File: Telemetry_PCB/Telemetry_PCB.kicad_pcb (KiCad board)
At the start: 2 copper layers, 27.9 x 18.5 mm, 7 parts, among them J1 Raspberry Pi Zero W, J2 Voltage Sensor, J3 Current Sensor, J4 ADC, J5 GPS

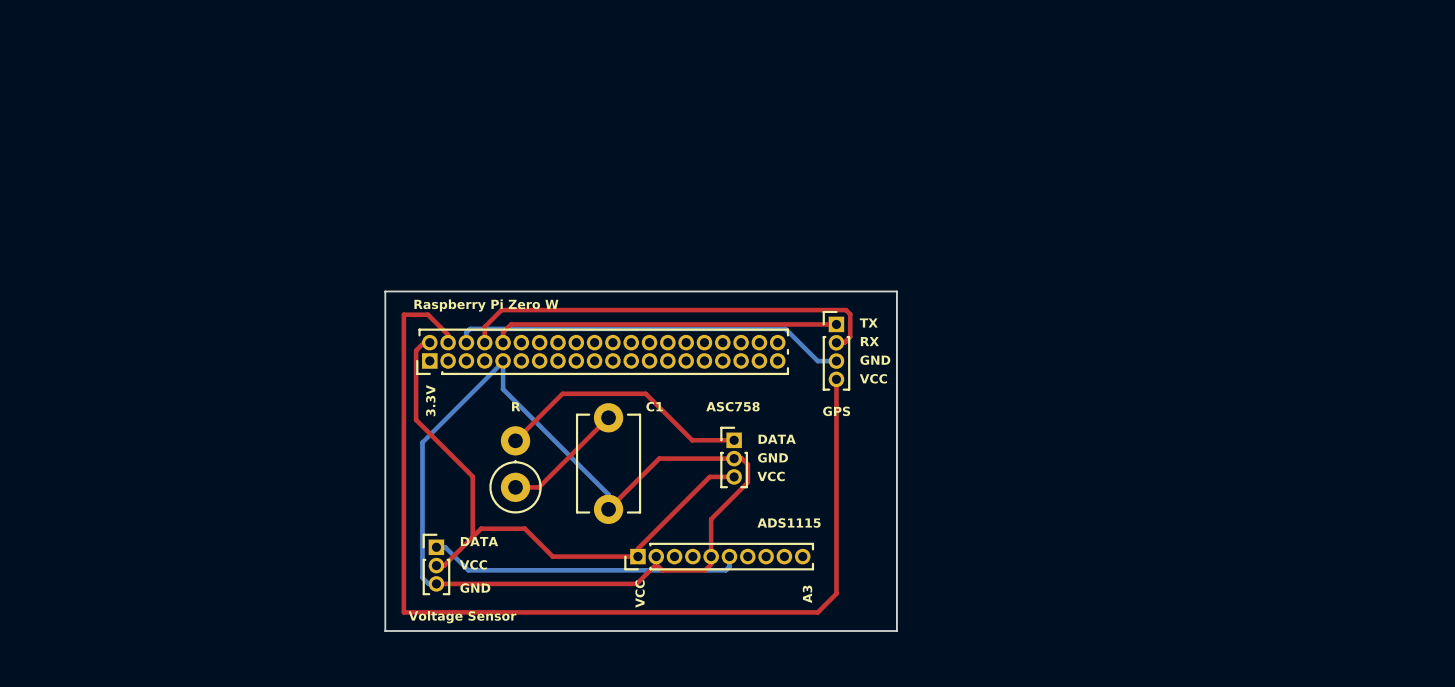
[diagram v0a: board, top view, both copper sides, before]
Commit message: Updated PCB Footprints
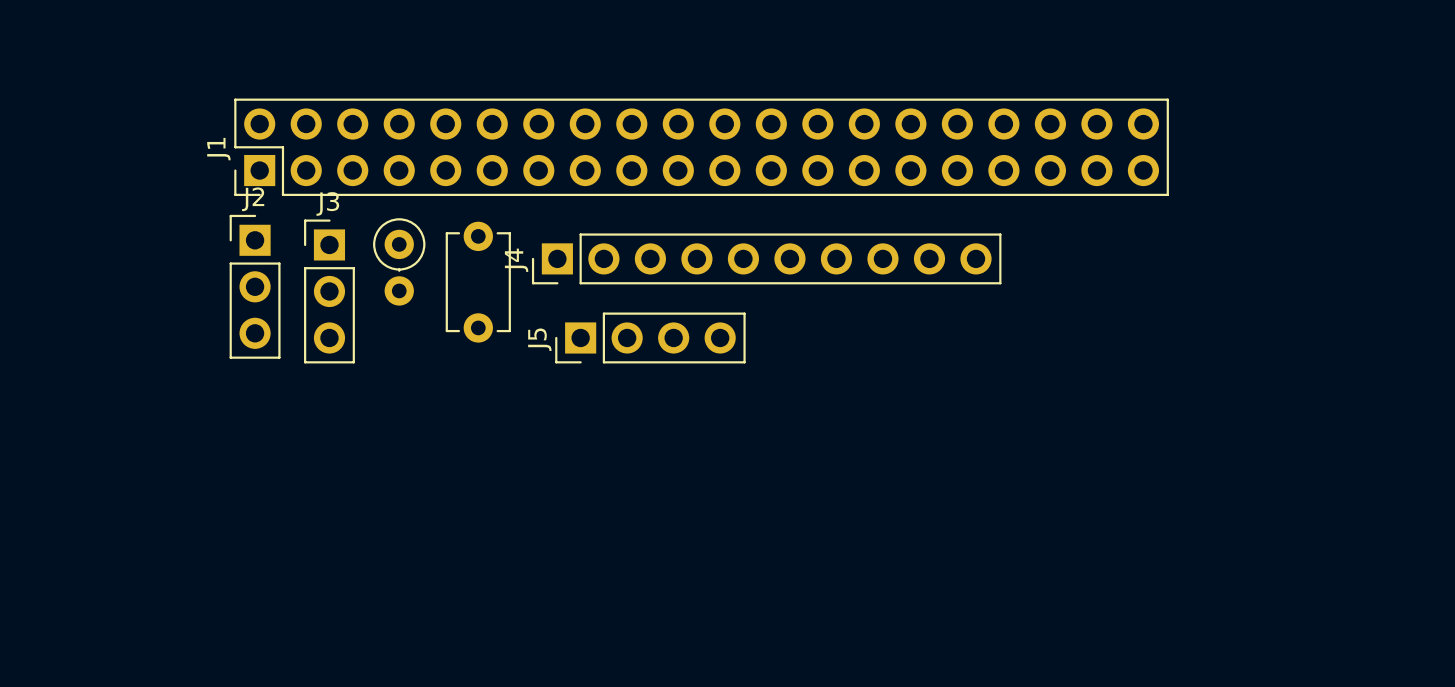
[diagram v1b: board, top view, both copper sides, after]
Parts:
- J1: footprint Connector_PinHeader_1.00mm:PinHeader_2x20_P1.00mm_Vertical -> Connector_PinHeader_2.54mm:PinHeader_2x20_P2.54mm_Vertical
- J2, J3: footprint Connector_PinHeader_1.00mm:PinHeader_1x03_P1.00mm_Vertical -> Connector_PinHeader_2.54mm:PinHeader_1x03_P2.54mm_Vertical
- J4: footprint Connector_PinHeader_1.00mm:PinHeader_1x10_P1.00mm_Vertical -> Connector_PinHeader_2.54mm:PinHeader_1x10_P2.54mm_Vertical
- J5: footprint Connector_PinHeader_1.00mm:PinHeader_1x04_P1.00mm_Vertical -> Connector_PinHeader_2.54mm:PinHeader_1x04_P2.54mm_Vertical
- moved J3 24.5 mm to (112.5, 64.5)
- moved J2 19.5 mm to (108.5, 64.3)
- moved J4 16.8 mm to (125.0, 65.3)
- moved R1 14.7 mm to (116.3, 64.5), turned to -90 degrees
- moved J5 14.0 mm to (126.2, 69.6), turned to 90 degrees
- moved J1 13.9 mm to (108.7, 60.5)
- moved C1 12.2 mm to (120.7, 69.0)
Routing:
- net Net-(J1-Pin_9): track 56.4 -> 0.00 mm
- net Net-(J1-Pin_4): track 55.3 -> 0.00 mm
- net Net-(J1-Pin_2): track 32.2 -> 0.00 mm
- net Net-(J1-Pin_8): track 23.4 -> 0.00 mm
- net Net-(J1-Pin_6): track 21.6 -> 0.00 mm
- net Net-(J1-Pin_10): track 18.9 -> 0.00 mm
- net Net-(J2-Pin_1): track 17.2 -> 0.00 mm
- net Net-(J3-Pin_1): track 14.1 -> 0.00 mm
- net Net-(J4-Pin_7): track 6.65 -> 0.00 mm
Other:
- board outline removed
- board text removed: "3.3V"
- board text removed: "A3"
- board text removed: "ADS1115"
- board text removed: "ASC758"
- board text removed: "C1"
- board text removed: "DATA"
- board text removed: "GND"
- board text removed: "GPS"
- board text removed: "R"
- board text removed: "RX"
- board text removed: "Raspberry Pi Zero W"
- board text removed: "TX"
- board text removed: "UMASS AMHERST 2023-2024 AERONAUTICS TEAM TELEMETRY SYSTEM"
- board text removed: "VCC"
- board text removed: "Voltage Sensor"

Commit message: Updated PCB Footprints
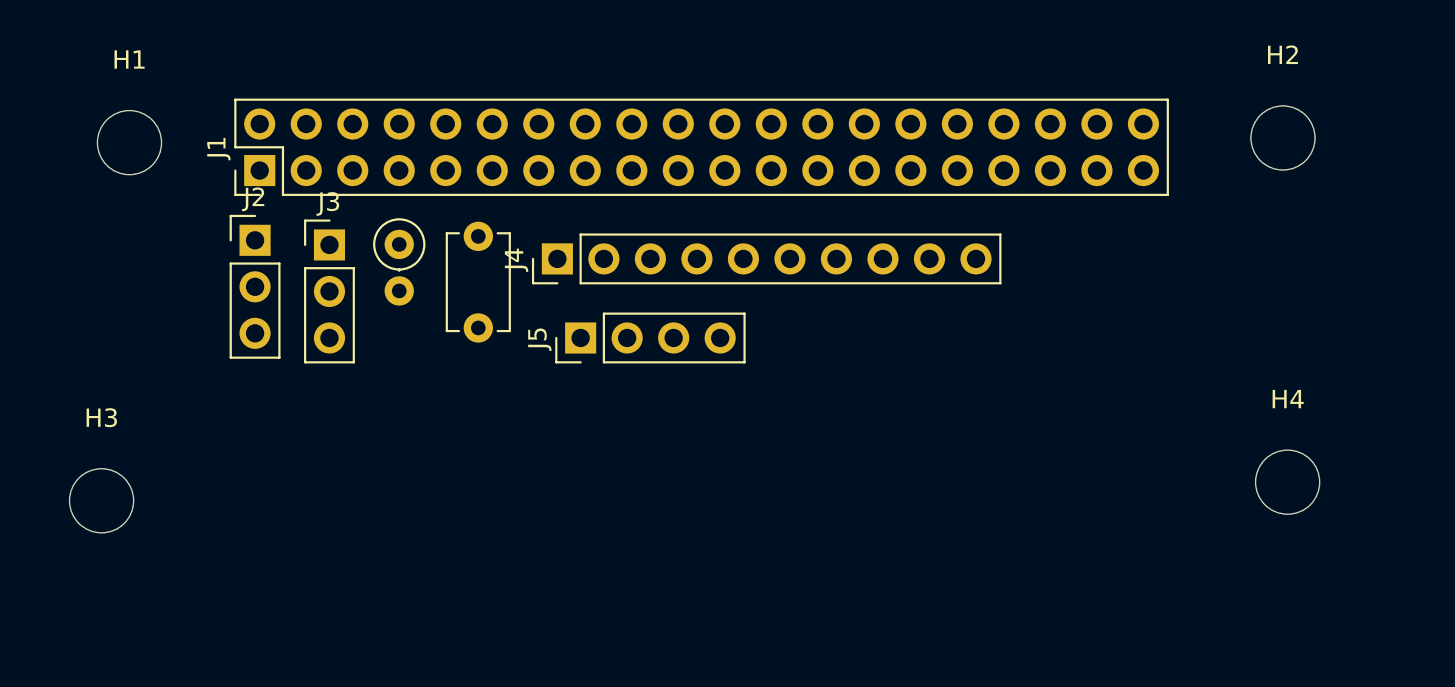
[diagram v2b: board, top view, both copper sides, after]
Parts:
- added H1: MountingHole, MountingHole:MountingHole_3.5mm, F.Cu at (101.6, 58.9)
- added H2: MountingHole, MountingHole:MountingHole_3.5mm, F.Cu at (164.6, 58.7)
- added H3: MountingHole, MountingHole:MountingHole_3.5mm, F.Cu at (100.1, 78.5)
- added H4: MountingHole, MountingHole:MountingHole_3.5mm, F.Cu at (164.8, 77.5)
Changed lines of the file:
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@@
   (net 45 "unconnected-(J4-Pin_9-Pad9)")
   (net 46 "unconnected-(J4-Pin_10-Pad10)")
+  (footprint "MountingHole:MountingHole_3.5mm" (layer "F.Cu")
+    (at 164.592 58.674)
+    (descr "Mounting Hole 3.5mm, no annular")
+    (tags "mounting hole 3.5mm no annular")
+    (property "Sheetfile" "Telemetry_PCB.kicad_sch")
+    (property "Sheetname" "")
+    (property "ki_description" "Mounting Hole without connection")
+    (property "ki_keywords" "mounting hole")
+    (attr exclude_from_pos_files)
+    (fp_text reference "H2" (at 0 -4.5) (layer "F.SilkS")
+        (effects (font (size 1 1) (thickness 0.15)))
+    )
+    (fp_text value "MountingHole" (at 0 4.5) (layer "F.Fab")
+        (effects (font (size 1 1) (thickness 0.15)))
+    )
+    (fp_text user "${REFERENCE}" (at 0 0) (layer "F.Fab")
+        (effects (font (size 1 1) (thickness 0.15)))
+    )
+    (fp_circle (center 0 0) (end 3.5 0)
+      (stroke (width 0.15) (type solid)) (fill none) (layer "Cmts.User"))
+    (fp_circle (center 0 0) (end 3.75 0)
+      (stroke (width 0.05) (type solid)) (fill none) (layer "F.CrtYd"))
+    (pad "" np_thru_hole circle (at 0 0) (size 3.5 3.5) (drill 3.5) (layers "*.Cu" "*.Mask"))
+  )
   (footprint "Connector_PinHeader_2.54mm:PinHeader_1x10_P2.54mm_Vertical" (layer "F.Cu")
     (at 124.968 65.278 90)
@@
     )
   )
+  (footprint "MountingHole:MountingHole_3.5mm" (layer "F.Cu")
+    (at 100.076 78.486)
+    (descr "Mounting Hole 3.5mm, no annular")
+    (tags "mounting hole 3.5mm no annular")
+    (property "Sheetfile" "Telemetry_PCB.kicad_sch")
+    (property "Sheetname" "")
+    (property "ki_description" "Mounting Hole without connection")
+    (property "ki_keywords" "mounting hole")
+    (attr exclude_from_pos_files)
+    (fp_text reference "H3" (at 0 -4.5) (layer "F.SilkS")
+        (effects (font (size 1 1) (thickness 0.15)))
+    )
+    (fp_text value "MountingHole" (at 0 4.5) (layer "F.Fab")
+        (effects (font (size 1 1) (thickness 0.15)))
+    )
+    (fp_text user "${REFERENCE}" (at 0 0) (layer "F.Fab")
+        (effects (font (size 1 1) (thickness 0.15)))
+    )
+    (fp_circle (center 0 0) (end 3.5 0)
+      (stroke (width 0.15) (type solid)) (fill none) (layer "Cmts.User"))
+    (fp_circle (center 0 0) (end 3.75 0)
+      (stroke (width 0.05) (type solid)) (fill none) (layer "F.CrtYd"))
+    (pad "" np_thru_hole circle (at 0 0) (size 3.5 3.5) (drill 3.5) (layers "*.Cu" "*.Mask"))
+  )
+  (footprint "MountingHole:MountingHole_3.5mm" (layer "F.Cu")
+    (at 101.6 58.928)
+    (descr "Mounting Hole 3.5mm, no annular")
+    (tags "mounting hole 3.5mm no annular")
+    (property "Sheetfile" "Telemetry_PCB.kicad_sch")
+    (property "Sheetname" "")
+    (property "ki_description" "Mounting Hole without connection")
+    (property "ki_keywords" "mounting hole")
+    (attr exclude_from_pos_files)
+    (fp_text reference "H1" (at 0 -4.5) (layer "F.SilkS")
+        (effects (font (size 1 1) (thickness 0.15)))
+    )
+    (fp_text value "MountingHole" (at 0 4.5) (layer "F.Fab")
+        (effects (font (size 1 1) (thickness 0.15)))
+    )
+    (fp_text user "${REFERENCE}" (at 0 0) (layer "F.Fab")
+        (effects (font (size 1 1) (thickness 0.15)))
+    )
+    (fp_circle (center 0 0) (end 3.5 0)
+      (stroke (width 0.15) (type solid)) (fill none) (layer "Cmts.User"))
+    (fp_circle (center 0 0) (end 3.75 0)
+      (stroke (width 0.05) (type solid)) (fill none) (layer "F.CrtYd"))
+    (pad "" np_thru_hole circle (at 0 0) (size 3.5 3.5) (drill 3.5) (layers "*.Cu" "*.Mask"))
+  )
   (footprint "Resistor_THT:R_Axial_DIN0207_L6.3mm_D2.5mm_P2.54mm_Vertical" (layer "F.Cu")
     (at 116.332 64.487 -90)
@@
     )
   )
+  (footprint "MountingHole:MountingHole_3.5mm" (layer "F.Cu")
+    (at 164.846 77.47)
+    (descr "Mounting Hole 3.5mm, no annular")
+    (tags "mounting hole 3.5mm no annular")
+    (property "Sheetfile" "Telemetry_PCB.kicad_sch")
+    (property "Sheetname" "")
+    (property "ki_description" "Mounting Hole without connection")
+    (property "ki_keywords" "mounting hole")
+    (attr exclude_from_pos_files)
+    (fp_text reference "H4" (at 0 -4.5) (layer "F.SilkS")
+        (effects (font (size 1 1) (thickness 0.15)))
+    )
+    (fp_text value "MountingHole" (at 0 4.5) (layer "F.Fab")
+        (effects (font (size 1 1) (thickness 0.15)))
+    )
+    (fp_text user "${REFERENCE}" (at 0 0) (layer "F.Fab")
+        (effects (font (size 1 1) (thickness 0.15)))
+    )
+    (fp_circle (center 0 0) (end 3.5 0)
+      (stroke (width 0.15) (type solid)) (fill none) (layer "Cmts.User"))
+    (fp_circle (center 0 0) (end 3.75 0)
+      (stroke (width 0.05) (type solid)) (fill none) (layer "F.CrtYd"))
+    (pad "" np_thru_hole circle (at 0 0) (size 3.5 3.5) (drill 3.5) (layers "*.Cu" "*.Mask"))
+  )
   (footprint "Connector_PinHeader_2.54mm:PinHeader_2x20_P2.54mm_Vertical" (layer "F.Cu")

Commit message: Adding email system
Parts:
- removed H4: MountingHole, MountingHole:MountingHole_3.5mm
- moved J3 45.0 mm to (157.5, 66.5)
- moved J2 31.9 mm to (137.9, 76.5), turned to 90 degrees
- moved J5 25.4 mm to (101.1, 73.4), turned to 180 degrees
- moved R1 24.0 mm to (140.2, 66.8), turned to 0 degrees
- moved J4 17.5 mm to (109.5, 73.4)
- moved C1 7.63 mm to (127.5, 65.8), turned to 0 degrees
- moved H3 3.67 mm to (101.3, 81.9)
- moved H2 2.02 mm to (166.6, 58.9)
- moved J1 1.30 mm to (110.0, 60.2)
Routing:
- net Net-(J1-Pin_9): track 0.00 -> 81.9 mm
- net Net-(J1-Pin_2): track 0.00 -> 67.8 mm
- net Net-(J1-Pin_10): track 0.00 -> 36.1 mm
- net Net-(J1-Pin_8): track 0.00 -> 29.8 mm
- net Net-(J1-Pin_6): track 0.00 -> 23.5 mm
- net Net-(J4-Pin_7): track 0.00 -> 19.0 mm
- net Net-(J2-Pin_1): track 0.00 -> 17.0 mm
- net Net-(J1-Pin_4): track 0.00 -> 16.5 mm
- net Net-(J3-Pin_1): track 0.00 -> 15.2 mm
- net Net-(J1-Pin_3): track 0.00 -> 15.1 mm
- net Net-(J1-Pin_5): track 0.00 -> 13.4 mm
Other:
- board outline added: 75.4 x 33 mm
- board text added: "A3"
- board text added: "ACS758"
- board text added: "C1"
- board text added: "G"
- board text added: "GND"
- board text added: "GPS"
- board text added: "R1"
- board text added: "RX"
- board text added: "Raspberry Pi Zero W"
- board text added: "S"
- board text added: "TX"
- board text added: "UMASS AERONAUTICS TELEMETRY 2023-2024"
- board text added: "V"
- board text added: "VCC"
